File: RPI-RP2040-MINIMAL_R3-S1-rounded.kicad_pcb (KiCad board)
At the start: 2 copper layers, 65 x 70.5 mm, 31 parts, among them J3 Conn_01x04_Pin, J4 Conn_01x04_Socket, P1 USB_C_Plug_USB2.0, U1 NCP1117ST33T3G, U2 W25Q128JVSIQ, U3 RP2040, X1 12MHz

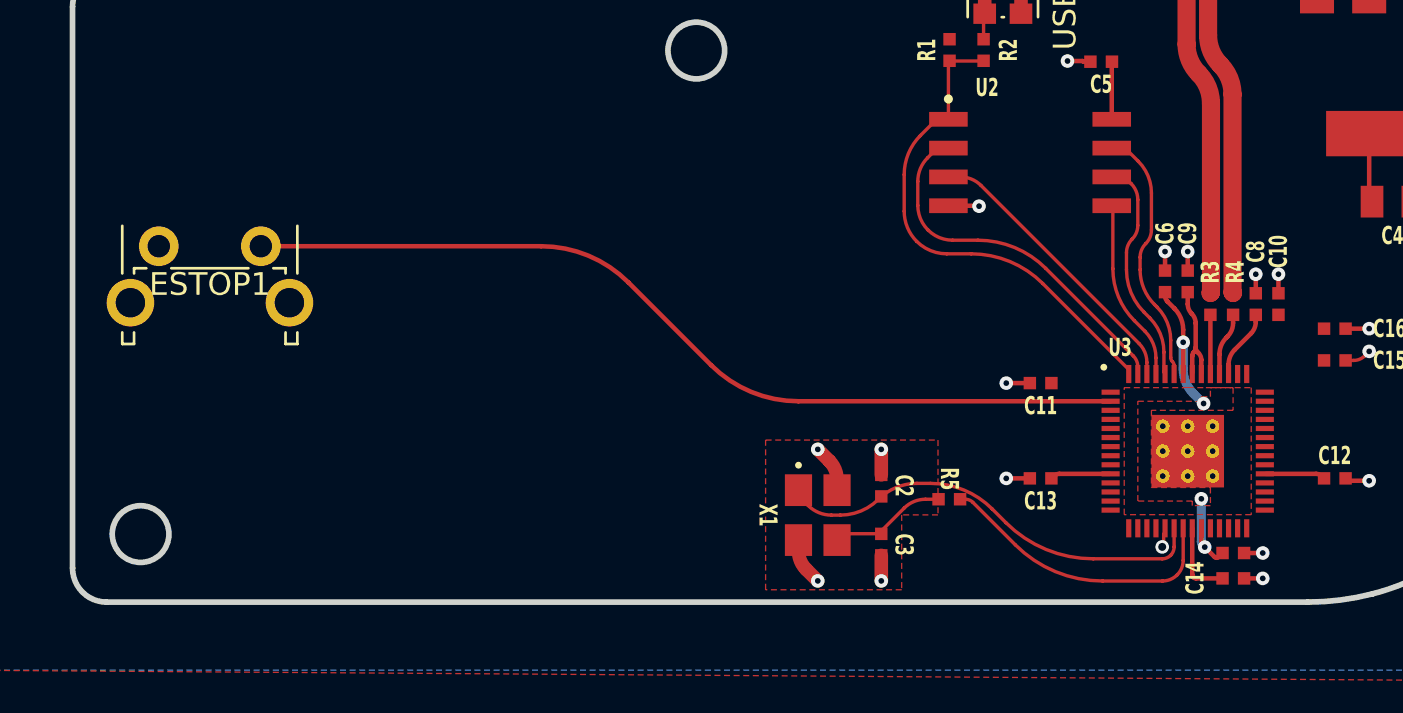
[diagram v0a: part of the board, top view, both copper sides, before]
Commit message: fix 1V1 connection
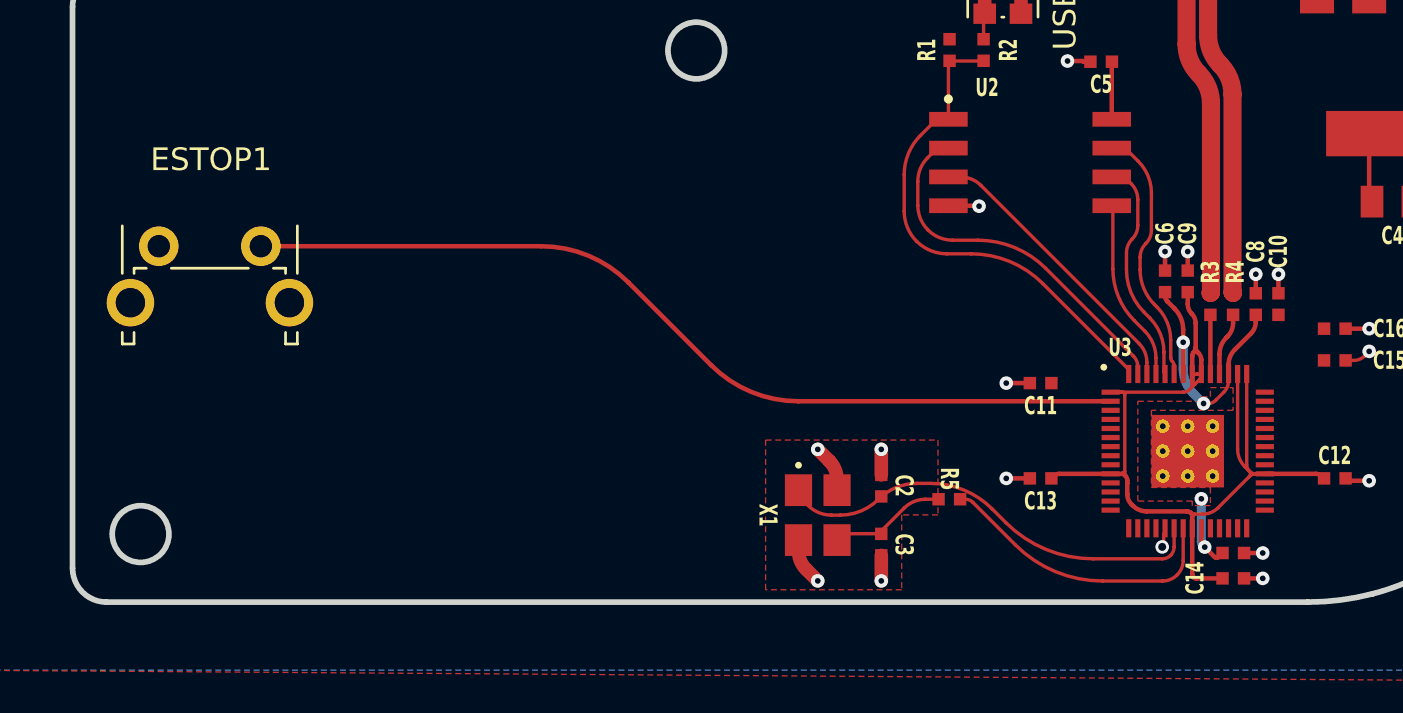
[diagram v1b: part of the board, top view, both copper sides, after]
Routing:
- net +3V3: track 19.3 -> 48.3 mm
- net +1V1: track 13.9 -> 15.8 mm
- added copper zone on F.Cu, net +1V1
- removed copper zone on F.Cu, net (none)

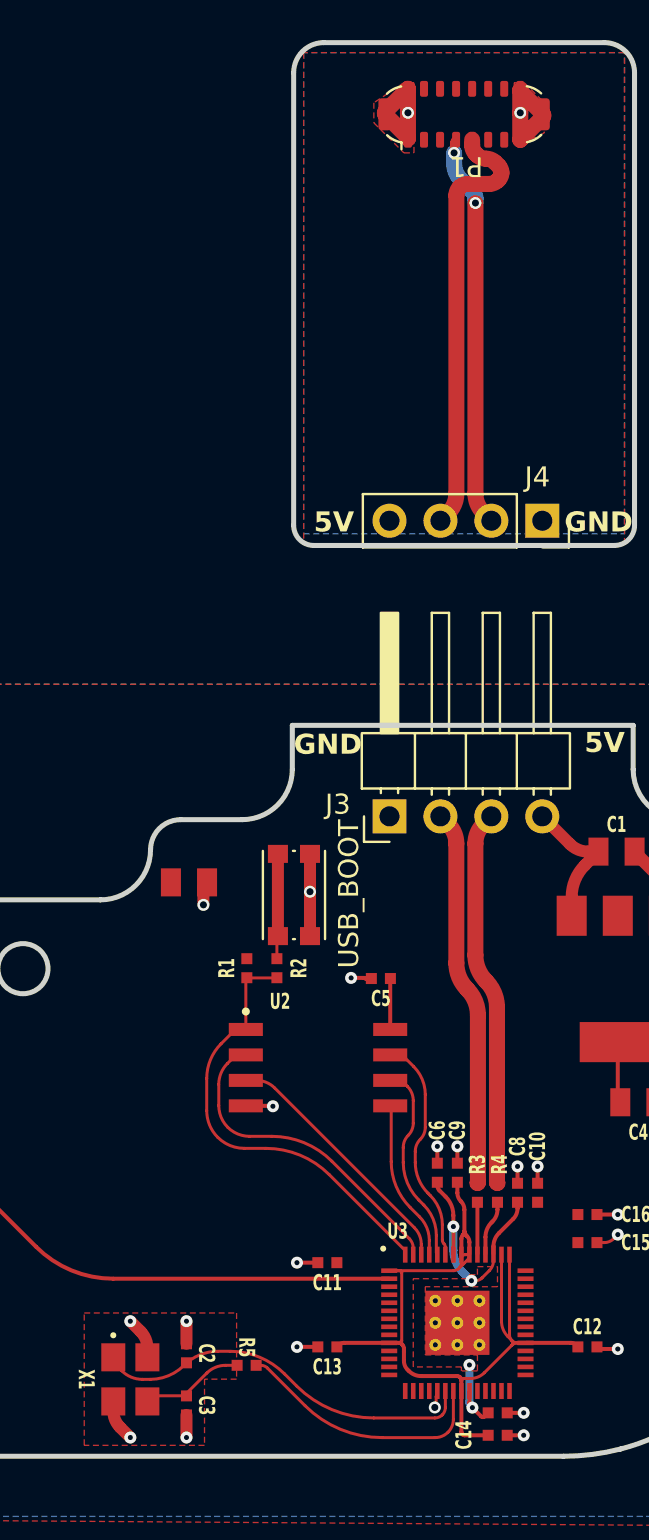
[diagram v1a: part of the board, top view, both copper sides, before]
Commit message: fix ground plane underneath crystal
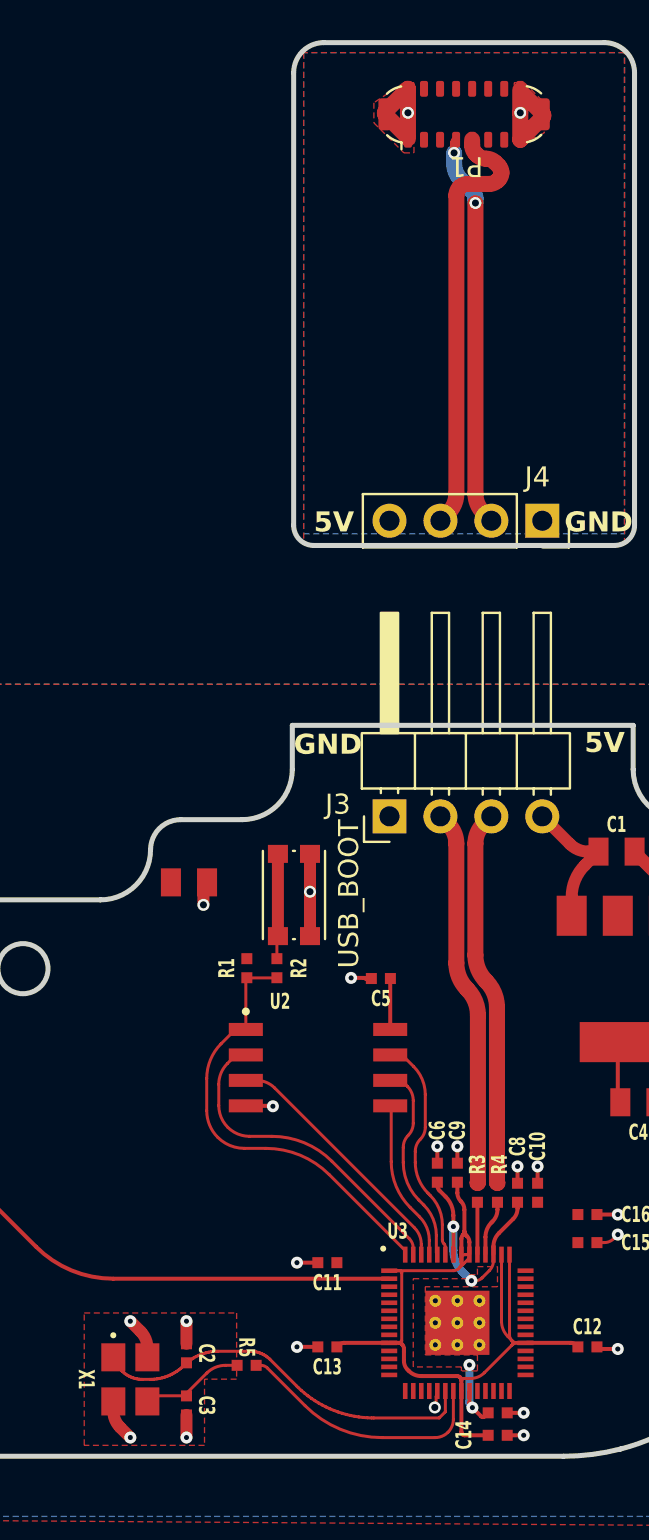
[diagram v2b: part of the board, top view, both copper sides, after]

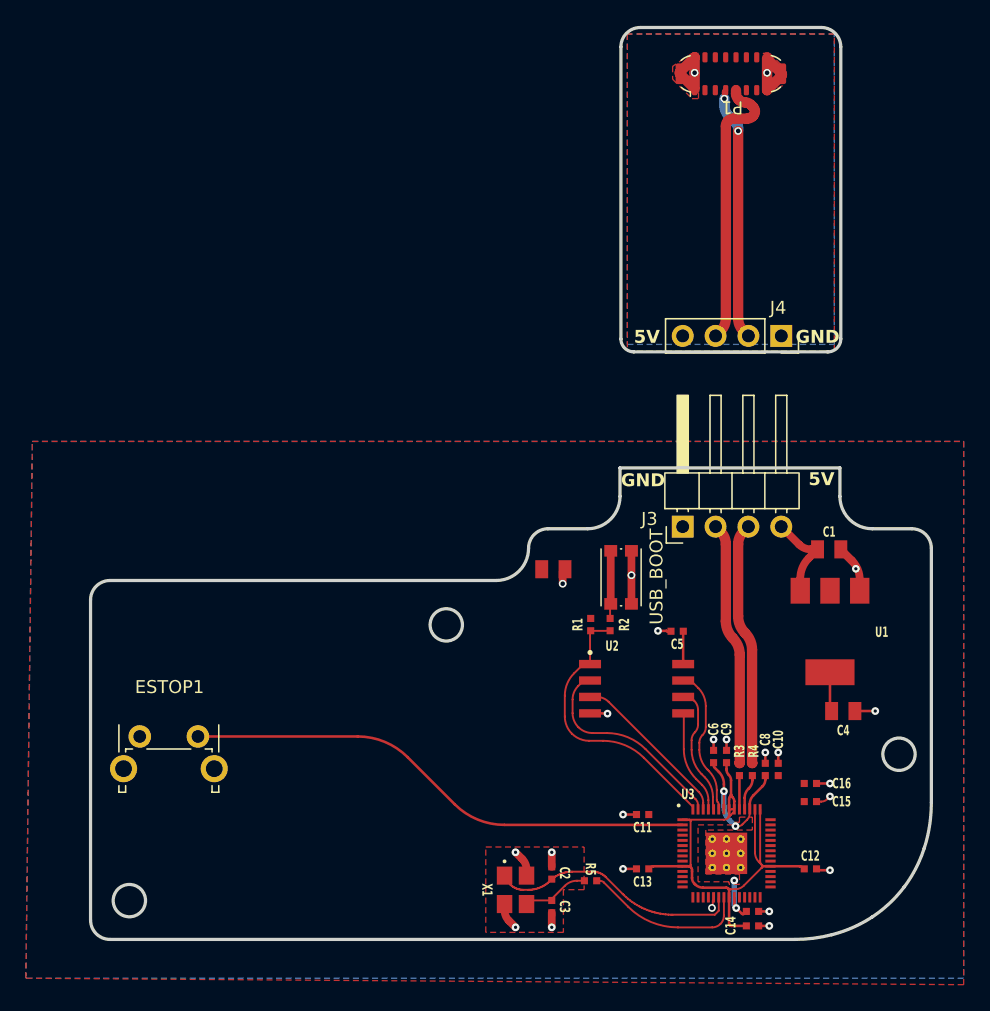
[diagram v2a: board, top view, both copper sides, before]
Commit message: fix offset + teardrops
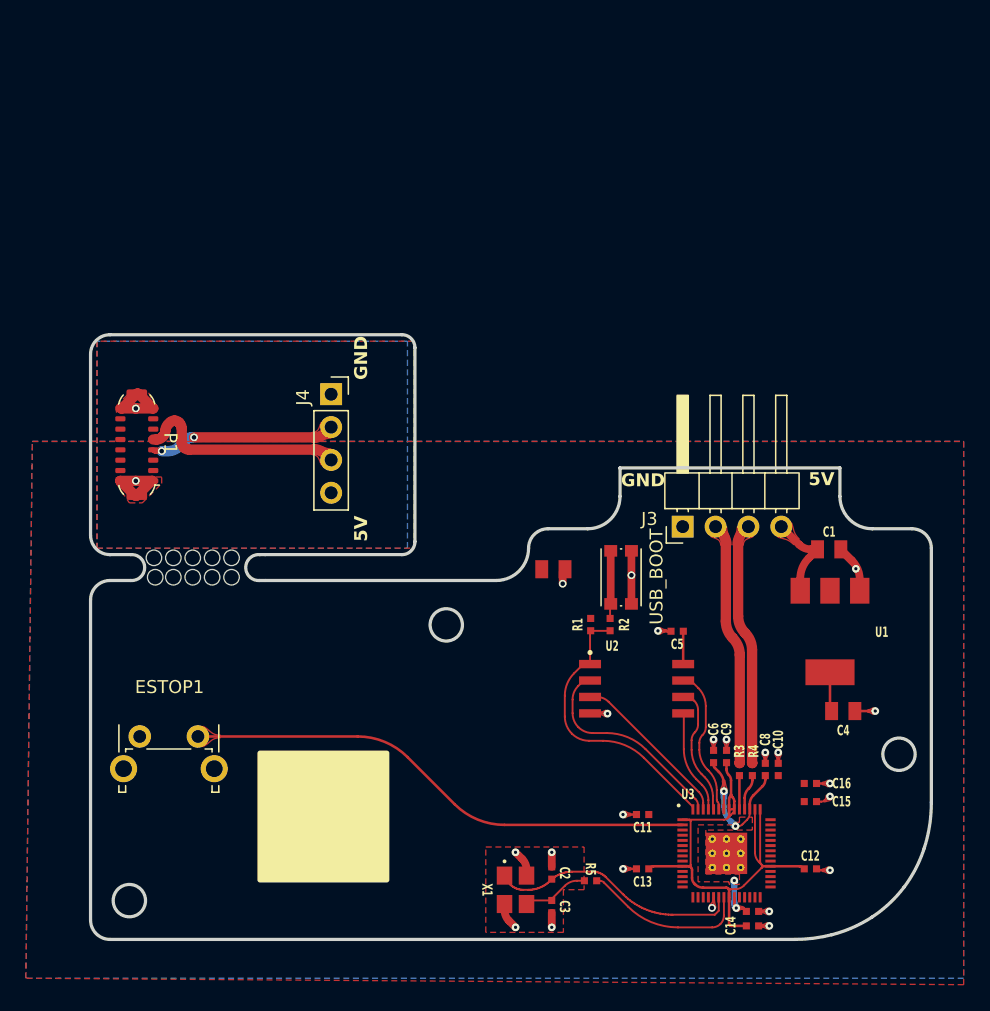
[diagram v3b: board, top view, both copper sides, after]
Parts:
- moved P1 54.1 mm to (54.1, 68.8), turned to 180 degrees
- moved J4 35.1 mm to (69.1, 64.9), turned to 0 degrees
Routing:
- net /BRIDGE_USBD+: track 19.7 -> 14.4 mm
- net /BRIDGE_USBD-: track 21.8 -> 16.6 mm
- net +1V1: track 15.8 -> 15.2 mm
- net /QSPI_SD2: track 12.8 -> 12.3 mm
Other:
- board size 65 x 70.5 mm -> 65 x 46.7 mm

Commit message: switch to 2mb flash + debug port
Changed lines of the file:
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@@
 		)
 	)
+	(gr_rect
+		(start 65 95)
+		(end 75 105)
+		(stroke
+			(width 0.12)
+			(type default)
+		)
+		(fill no)
+		(layer "F.SilkS")
+	)
 	(gr_line
 		(start 50.5 61.7517)
@@
 		)
 	)
-	(zone
-		(layer "F.SilkS")
-		(hatch edge 0.508)
-		(connect_pads yes
-			(clearance 0)
-		)
-		(min_thickness 0.2)
-		(fill yes
-			(thermal_gap 0.3)
-			(thermal_bridge_width 0.3)
-			(island_removal_mode 0)
-		)
-		(polygon
-			(pts
-				(xy 73.5 92.5) (xy 63.5 92.5) (xy 63.5 102.5) (xy 73.5 102.5)
-			)
-		)
-	)
 	(group ""
 		(members "7030e1ae-2083-4e0c-b310-6d0bb6cff4db" "71e8feaa-ad86-4fff-ad70-0ec18ffcd9e4"
-			"75b64f6e-cabd-4898-9bc3-e9c8d97c8368" "86904204-f297-4165-9239-305653056d9d"
-			"8a055d9b-cff1-4a25-8f95-e32bc02e42eb" "8ab97694-2f58-485c-b18e-a6ffee00ea84"
-			"96195365-365b-4246-ad06-d37062c93fe3" "96b7201e-1eaf-4251-9978-d0425f73d9f5"
-			"9711f30b-6031-4524-9bf1-3bb795aa0915" "a43971be-2932-40ed-909f-1ccc4ce9f7d0"
-			"a83b520f-0de3-44e5-8523-669a51519cc3" "a99811d5-4d79-4925-9e62-cd4e3308589b"
-			"bb80e3a1-be2f-4f57-836c-e9777ddf31bc" "c9b54a73-55b4-4a13-b75f-a99519f7eb76"
-			"d5cff7bb-9d67-4bc1-a76e-e58f62ce7cbf" "dfc72a59-37ad-4371-bd75-ba64bde0549d"
-			"ec729c32-55b1-4b8e-a035-bd5ab4f56213" "f4ae312d-250b-4c3b-8e96-93bde8e4b53c"
+			"75b64f6e-cabd-4898-9bc3-e9c8d97c8368" "8a055d9b-cff1-4a25-8f95-e32bc02e42eb"
+			"8ab97694-2f58-485c-b18e-a6ffee00ea84" "96195365-365b-4246-ad06-d37062c93fe3"
+			"96b7201e-1eaf-4251-9978-d0425f73d9f5" "9711f30b-6031-4524-9bf1-3bb795aa0915"
+			"a43971be-2932-40ed-909f-1ccc4ce9f7d0" "a83b520f-0de3-44e5-8523-669a51519cc3"
+			"a99811d5-4d79-4925-9e62-cd4e3308589b" "bb80e3a1-be2f-4f57-836c-e9777ddf31bc"
+			"c9b54a73-55b4-4a13-b75f-a99519f7eb76" "d5cff7bb-9d67-4bc1-a76e-e58f62ce7cbf"
+			"dfc72a59-37ad-4371-bd75-ba64bde0549d" "ec729c32-55b1-4b8e-a035-bd5ab4f56213"
+			"f4ae312d-250b-4c3b-8e96-93bde8e4b53c"
 		)
 	)

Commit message: teardrops
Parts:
- added J1: Conn_01x03_Socket, Connector_PinHeader_1.00mm:PinHeader_1x03_P1.00mm_Vertical, F.Cu at (106.5, 104.3)
- added R6: 100, Resistor_SMD:R_0402_1005Metric, F.Cu at (104.5, 105.2)
- added R7: 100, Resistor_SMD:R_0402_1005Metric, F.Cu at (104.5, 104.2)
- moved C14 2.85 mm to (98.8, 106.0), turned to 180 degrees
- moved C7 1.20 mm to (101.7, 106.0)
- moved J4 0.09 mm to (69.1, 64.8)
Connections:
- P1 pad B6: (no net) -> /BRIDGE_USBD+
- P1 pad B7: (no net) -> /BRIDGE_USBD-
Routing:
- net /BRIDGE_USBD+: track 14.4 -> 21.7 mm, vias 2 -> 3
- net /BRIDGE_USBD-: track 16.6 -> 23.5 mm
- net /SWCLK: track 0.00 -> 4.15 mm
- net Net-(J1-Pin_3): track 0.00 -> 3.97 mm
- net /SWD: track 0.00 -> 3.57 mm
- net +1V1: track 15.2 -> 17.1 mm
- net Net-(J1-Pin_1): track 0.00 -> 1.86 mm
- net +3V3: track 48.0 -> 47.3 mm
- net /QSPI_SD2: track 12.3 -> 12.8 mm
- net /XOUT: track 12.9 -> 12.4 mm
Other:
- board text added: "C G D"
- board text added: "DEBUG"
